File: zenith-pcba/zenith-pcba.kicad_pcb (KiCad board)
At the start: 2 copper layers, 194.1 x 141.7 mm, 63 parts, among them SW1 G4R152312, U1 XC7K70T-FBG676, U10 TXS0101DB, U2 K4B4G1646E-BCNB, U3 CH347T, U4 AP63203WU, U5 TXS0101DB, U6 TXS0101DB, U7 TXS0101DB, U8 TXS0101DB, U9 TXS0101DB, X1 SX5B8.000F1520F30

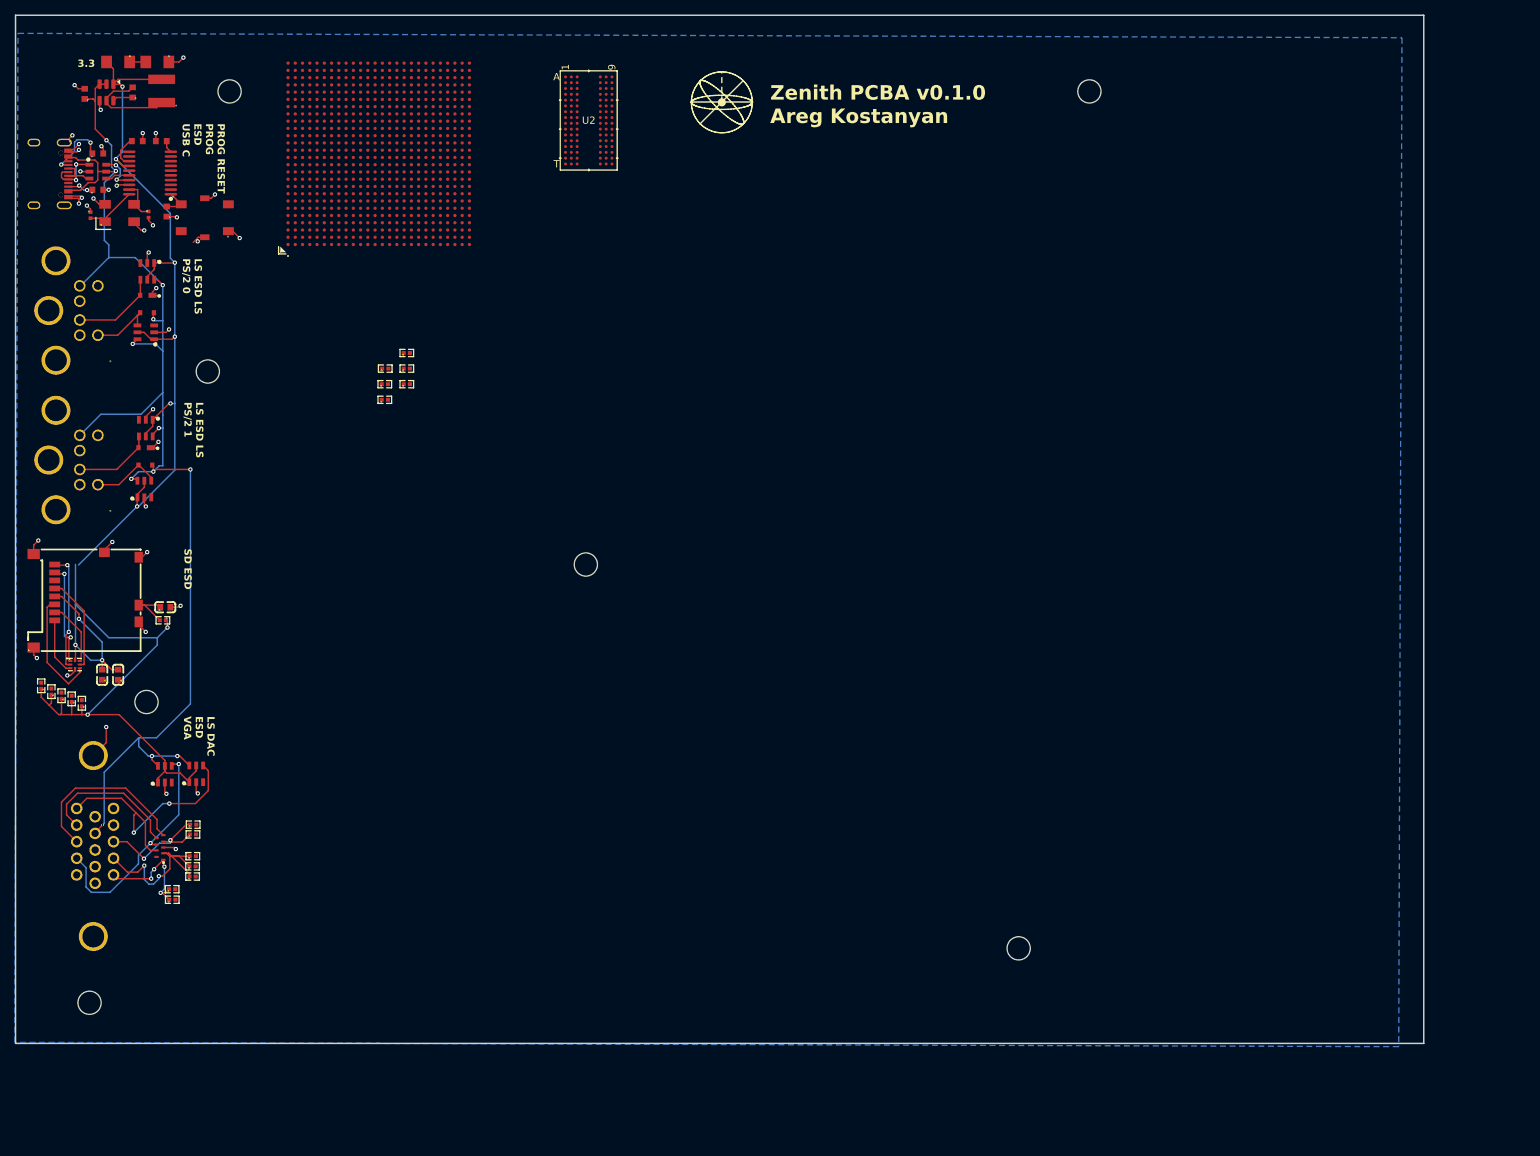
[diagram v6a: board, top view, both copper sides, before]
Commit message: feat(hardware): ddr3 sodimm import
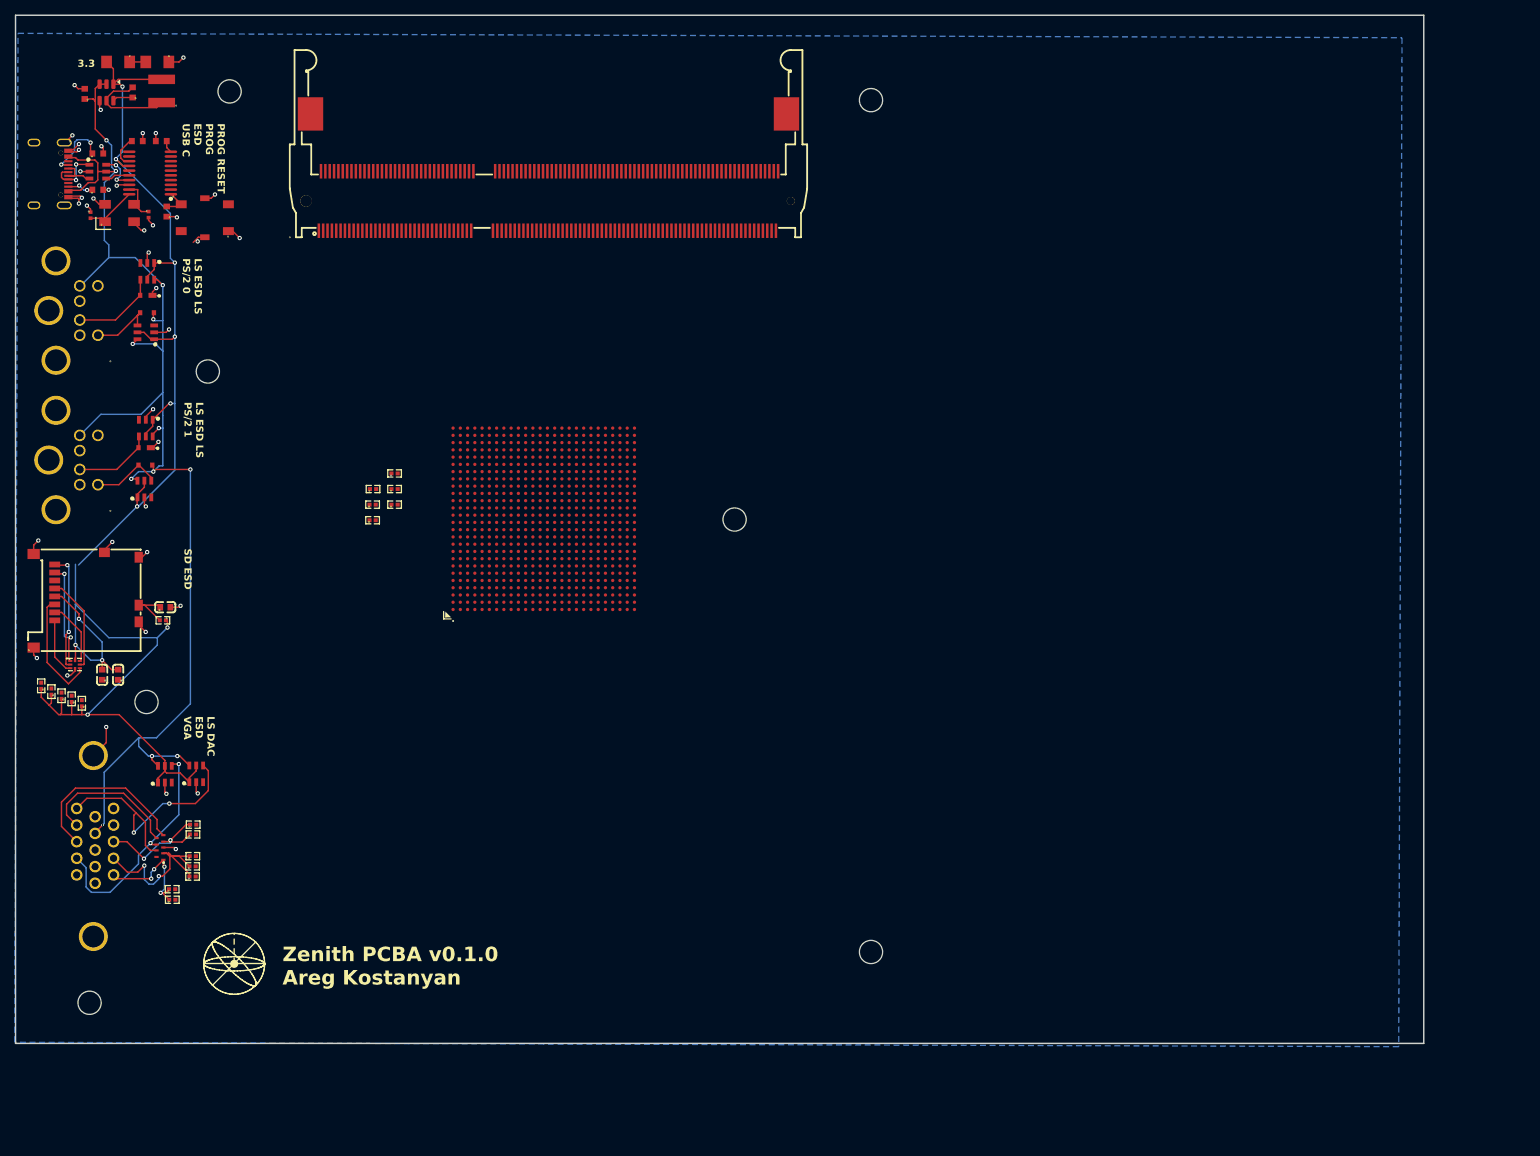
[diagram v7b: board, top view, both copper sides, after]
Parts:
- removed U2: K4B4G1646E-BCNB, footprints:BGA96_K4B4G1_SAM
- added CN1: AS0A621-H2S6-7H, easyeda2kicad:CONN-SMD_204P-P0.60_AS0A621-H2S6-7H, F.Cu at (112.5, 36.4)
- moved U1 55.2 mm to (111.9, 84.1)
- moved REF** 30.1 mm to (157.0, 26.4)
- moved REF** 21.4 mm to (138.2, 84.2)
- moved REF** 20.4 mm to (157.0, 143.8)
- moved R11 16.7 mm to (88.3, 82.2)
- moved R15 16.7 mm to (91.3, 82.2)
- moved R10 16.7 mm to (88.4, 80.0)
- moved R14 16.7 mm to (91.3, 80.0)
- moved R12 16.7 mm to (88.3, 84.3)
- moved R13 16.7 mm to (91.3, 77.8)
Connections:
- U1 pad A17: unconnected-(U1B-IO_L3N_T0_DQS_AD1N_15-PadA17) -> DDR3_DQS0_N
- U1 pad A18: unconnected-(U1B-IO_L2P_T0_AD8P_15-PadA18) -> DDR3_DQ1
- U1 pad A19: unconnected-(U1B-IO_L2N_T0_AD8N_15-PadA19) -> DDR3_DQ2
- U1 pad A20: unconnected-(U1B-IO_L8N_T1_D12_14-PadA20) -> DDR3_A10
- U1 pad B16: unconnected-(U1B-IO_L1N_T0_AD0N_15-PadB16) -> DDR3_DQ0
- U1 pad B17: unconnected-(U1B-IO_L3P_T0_DQS_AD1P_15-PadB17) -> DDR3_DQS0_P
- U1 pad B19: unconnected-(U1B-IO_L4N_T0_AD9N_15-PadB19) -> DDR3_DQ4
- U1 pad B20: unconnected-(U1B-IO_L8P_T1_D11_14-PadB20) -> DDR3_A11
- U1 pad B21: unconnected-(U1B-IO_L10N_T1_D15_14-PadB21) -> DDR3_A6
- U1 pad C16: unconnected-(U1B-IO_L1P_T0_AD0P_15-PadC16) -> DDR3_DM0
- U1 pad C17: unconnected-(U1B-IO_L5P_T0_AD2P_15-PadC17) -> DDR3_DQ5
- U1 pad C18: unconnected-(U1B-IO_L5N_T0_AD2N_15-PadC18) -> DDR3_DQ6
- U1 pad C19: unconnected-(U1B-IO_L4P_T0_AD9P_15-PadC19) -> DDR3_DQ3
- U1 pad C21: unconnected-(U1B-IO_L10P_T1_D14_14-PadC21) -> DDR3_A7
- U1 pad C22: unconnected-(U1B-IO_L7N_T1_D10_14-PadC22) -> DDR3_A12
- U1 pad D15: unconnected-(U1B-IO_L6P_T0_15-PadD15) -> DDR3_DQ7
- U1 pad D18: unconnected-(U1B-IO_L13N_T2_MRCC_15-PadD18) -> DDR3_DQ17
- U1 pad D19: unconnected-(U1B-IO_L15P_T2_DQS_15-PadD19) -> DDR3_DQS2_P
- U1 pad D20: unconnected-(U1B-IO_L15N_T2_DQS_ADV_B_15-PadD20) -> DDR3_DQS2_N
- U1 pad D21: unconnected-(U1B-IO_L7P_T1_D09_14-PadD21) -> DDR3_A13
- U1 pad D23: unconnected-(U1B-IO_L11P_T1_SRCC_14-PadD23) -> DDR3_A5
- U1 pad D24: unconnected-(U1B-IO_L11N_T1_SRCC_14-PadD24) -> DDR3_A4
- U1 pad D25: unconnected-(U1B-IO_L15N_T2_DQS_DOUT_CSO_B_14-PadD25) -> DDR3_BA1
- U1 pad E15: unconnected-(U1B-IO_L10P_T1_AD4P_15-PadE15) -> DDR3_DQ11
- U1 pad E16: unconnected-(U1B-IO_L10N_T1_AD4N_15-PadE16) -> DDR3_DQ12
- U1 pad E17: unconnected-(U1B-IO_L12N_T1_MRCC_AD5N_15-PadE17) -> DDR3_RESET_N
- U1 pad E18: unconnected-(U1B-IO_L13P_T2_MRCC_15-PadE18) -> DDR3_DQ16
- U1 pad E20: unconnected-(U1B-IO_L17N_T2_A25_15-PadE20) -> DDR3_DQ22
- U1 pad E21: unconnected-(U1B-IO_L9P_T1_DQS_14-PadE21) -> DDR3_A9
- U1 pad E22: unconnected-(U1B-IO_L9N_T1_DQS_D13_14-PadE22) -> DDR3_A8
- U1 pad E23: unconnected-(U1B-IO_L12N_T1_MRCC_14-PadE23) -> DDR3_A2
- U1 pad E25: unconnected-(U1B-IO_L15P_T2_DQS_RDWR_B_14-PadE25) -> DDR3_BA2
- U1 pad E26: unconnected-(U1B-IO_L17N_T2_A13_D29_14-PadE26) -> DDR3_WE_N
- U1 pad F15: unconnected-(U1B-IO_L8N_T1_AD3N_15-PadF15) -> DDR3_DQ10
- U1 pad F17: unconnected-(U1B-IO_L12P_T1_MRCC_AD5P_15-PadF17) -> DDR3_DQ15
- U1 pad F18: unconnected-(U1B-IO_L11N_T1_SRCC_AD12N_15-PadF18) -> DDR3_DQ14
- U1 pad F19: unconnected-(U1B-IO_L17P_T2_A26_15-PadF19) -> DDR3_DQ21
- U1 pad F20: unconnected-(U1B-IO_L16N_T2_A27_15-PadF20) -> DDR3_DQ20
- U1 pad F22: unconnected-(U1B-IO_L12P_T1_MRCC_14-PadF22) -> DDR3_A3
- U1 pad F24: unconnected-(U1B-IO_L14N_T2_SRCC_14-PadF24) -> DDR3_A0
- U1 pad F25: unconnected-(U1B-IO_L17P_T2_A14_D30_14-PadF25) -> DDR3_CAS_N
- U1 pad G15: unconnected-(U1B-IO_L8P_T1_AD3P_15-PadG15) -> DDR3_DQ9
- U1 pad G16: unconnected-(U1B-IO_L7N_T1_AD10N_15-PadG16) -> DDR3_DQ8
- U1 pad G17: unconnected-(U1B-IO_L11P_T1_SRCC_AD12P_15-PadG17) -> DDR3_DQ13
- U1 pad G19: unconnected-(U1B-IO_L16P_T2_A28_15-PadG19) -> DDR3_DM2
- U1 pad G24: unconnected-(U1B-IO_L14P_T2_SRCC_14-PadG24) -> DDR3_A1
- U1 pad G25: unconnected-(U1B-IO_L16P_T2_CSI_B_14-PadG25) -> DDR3_BA0
- U1 pad G26: unconnected-(U1B-IO_L16N_T2_A15_D31_14-PadG26) -> DDR3_RAS_N
- U1 pad H16: unconnected-(U1B-IO_L7P_T1_AD10P_15-PadH16) -> DDR3_DM1
- U1 pad H17: unconnected-(U1B-IO_L14P_T2_SRCC_15-PadH17) -> DDR3_DQ18
- U1 pad H18: unconnected-(U1B-IO_L14N_T2_SRCC_15-PadH18) -> DDR3_DQ19
- U1 pad H19: unconnected-(U1B-IO_L18P_T2_A24_15-PadH19) -> DDR3_DQ23
- U1 pad H21: unconnected-(U1B-IO_L19P_T3_A10_D26_14-PadH21) -> DDR3_ODT
- U1 pad H22: unconnected-(U1B-IO_L21N_T3_DQS_A06_D22_14-PadH22) -> DDR3_CK_N
- U1 pad H26: unconnected-(U1B-IO_L18N_T2_A11_D27_14-PadH26) -> DDR3_CKE
- U1 pad J15: unconnected-(U1B-IO_L9P_T1_DQS_AD11P_15-PadJ15) -> DDR3_DQS1_P
- U1 pad J16: unconnected-(U1B-IO_L9N_T1_DQS_AD11N_15-PadJ16) -> DDR3_DQS1_N
- U1 pad J18: unconnected-(U1B-IO_L20P_T3_A20_15-PadJ18) -> DDR3_DQ24
- U1 pad J19: unconnected-(U1B-IO_L20N_T3_A19_15-PadJ19) -> DDR3_DQ25
- U1 pad J21: unconnected-(U1B-IO_L21P_T3_DQS_14-PadJ21) -> DDR3_CK_P
- U1 pad J26: unconnected-(U1B-IO_L18P_T2_A12_D28_14-PadJ26) -> DDR3_CS_N
- U1 pad K16: unconnected-(U1B-IO_L22P_T3_A17_15-PadK16) -> DDR3_DQ26
- U1 pad K17: unconnected-(U1B-IO_L22N_T3_A16_15-PadK17) -> DDR3_DQ27
- U1 pad K18: unconnected-(U1B-IO_L24N_T3_RS0_15-PadK18) -> DDR3_DQ31
- U1 pad K20: unconnected-(U1B-IO_L19P_T3_A22_15-PadK20) -> DDR3_DM3
- U1 pad K25: unconnected-(U1A-IO_L1P_T0_13-PadK25) -> DDR3_DM4
- U1 pad K26: unconnected-(U1A-IO_L1N_T0_13-PadK26) -> DDR3_DQ32
- U1 pad L17: unconnected-(U1B-IO_L24P_T3_RS1_15-PadL17) -> DDR3_DQ30
- U1 pad L18: unconnected-(U1B-IO_L23N_T3_FWE_B_15-PadL18) -> DDR3_DQ29
- U1 pad L19: unconnected-(U1B-IO_L21P_T3_DQS_15-PadL19) -> DDR3_DQS3_P
- U1 pad L20: unconnected-(U1B-IO_L21N_T3_DQS_A18_15-PadL20) -> DDR3_DQS3_N
- U1 pad L24: unconnected-(U1A-IO_L8N_T1_13-PadL24) -> DDR3_DQ42
- U1 pad L25: unconnected-(U1A-IO_L3N_T0_DQS_13-PadL25) -> DDR3_DQS4_N
- U1 pad M17: unconnected-(U1B-IO_L23P_T3_FOE_B_15-PadM17) -> DDR3_DQ28
- U1 pad M19: unconnected-(U1A-IO_L22N_T3_13-PadM19) -> DDR3_DQ59
- U1 pad M20: unconnected-(U1A-IO_L7N_T1_13-PadM20) -> DDR3_DQ40
- U1 pad M21: unconnected-(U1A-IO_L10P_T1_13-PadM21) -> DDR3_DQ43
- U1 pad M22: unconnected-(U1A-IO_L10N_T1_13-PadM22) -> DDR3_DQ44
- U1 pad M24: unconnected-(U1A-IO_L8P_T1_13-PadM24) -> DDR3_DQ41
- U1 pad M25: unconnected-(U1A-IO_L3P_T0_DQS_13-PadM25) -> DDR3_DQS4_P
- U1 pad M26: unconnected-(U1A-IO_L5N_T0_13-PadM26) -> DDR3_DQ38
- U1 pad N17: unconnected-(U1A-IO_L20N_T3_13-PadN17) -> DDR3_DQ57
- U1 pad N18: unconnected-(U1A-IO_L22P_T3_13-PadN18) -> DDR3_DQ58
- U1 pad N19: unconnected-(U1A-IO_L7P_T1_13-PadN19) -> DDR3_DM5
- U1 pad N21: unconnected-(U1A-IO_L12P_T1_MRCC_13-PadN21) -> DDR3_DQ47
- U1 pad N23: unconnected-(U1A-IO_L11N_T1_SRCC_13-PadN23) -> DDR3_DQ46
- U1 pad N24: unconnected-(U1A-IO_L4N_T0_13-PadN24) -> DDR3_DQ36
- U1 pad N26: unconnected-(U1A-IO_L5P_T0_13-PadN26) -> DDR3_DQ37
- U1 pad P16: unconnected-(U1A-IO_L20P_T3_13-PadP16) -> DDR3_DQ56
- U1 pad P18: unconnected-(U1A-IO_L24N_T3_13-PadP18) -> DDR3_DQ63
- U1 pad P19: unconnected-(U1A-IO_L9P_T1_DQS_13-PadP19) -> DDR3_DQS5_P
- U1 pad P20: unconnected-(U1A-IO_L9N_T1_DQS_13-PadP20) -> DDR3_DQS5_N
- U1 pad P21: unconnected-(U1A-IO_L13N_T2_MRCC_13-PadP21) -> DDR3_DQ49
- U1 pad P23: unconnected-(U1A-IO_L11P_T1_SRCC_13-PadP23) -> DDR3_DQ45
- U1 pad P24: unconnected-(U1A-IO_L4P_T0_13-PadP24) -> DDR3_DQ35
- U1 pad P26: unconnected-(U1A-IO_L2N_T0_13-PadP26) -> DDR3_DQ34
- U1 pad R16: unconnected-(U1A-IO_L21P_T3_DQS_13-PadR16) -> DDR3_DQS7_P
- U1 pad R17: unconnected-(U1A-IO_L21N_T3_DQS_13-PadR17) -> DDR3_DQS7_N
- U1 pad R18: unconnected-(U1A-IO_L24P_T3_13-PadR18) -> DDR3_DQ62
- U1 pad R20: unconnected-(U1A-IO_L16N_T2_13-PadR20) -> DDR3_DQ52
- U1 pad R21: unconnected-(U1A-IO_L13P_T2_MRCC_13-PadR21) -> DDR3_DQ48
- U1 pad R22: unconnected-(U1A-IO_L14P_T2_SRCC_13-PadR22) -> DDR3_DQ50
- U1 pad R23: unconnected-(U1A-IO_L14N_T2_SRCC_13-PadR23) -> DDR3_DQ51
- U1 pad R25: unconnected-(U1A-IO_L6P_T0_13-PadR25) -> DDR3_DQ39
- U1 pad R26: unconnected-(U1A-IO_L2P_T0_13-PadR26) -> DDR3_DQ33
- U1 pad T17: unconnected-(U1A-IO_L23N_T3_13-PadT17) -> DDR3_DQ61
- U1 pad T18: unconnected-(U1A-IO_L19P_T3_13-PadT18) -> DDR3_DM7
- U1 pad T20: unconnected-(U1A-IO_L16P_T2_13-PadT20) -> DDR3_DM6
- U1 pad T22: unconnected-(U1A-IO_L17P_T2_13-PadT22) -> DDR3_DQ53
- U1 pad T23: unconnected-(U1A-IO_L17N_T2_13-PadT23) -> DDR3_DQ54
- U1 pad T24: unconnected-(U1A-IO_L15P_T2_DQS_13-PadT24) -> DDR3_DQS6_P
- U1 pad T25: unconnected-(U1A-IO_L15N_T2_DQS_13-PadT25) -> DDR3_DQS6_N
- U1 pad U17: unconnected-(U1A-IO_L23P_T3_13-PadU17) -> DDR3_DQ60
- U1 pad U19: unconnected-(U1A-IO_L18P_T2_13-PadU19) -> DDR3_DQ55
